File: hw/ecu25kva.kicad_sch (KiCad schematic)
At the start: 0 parts

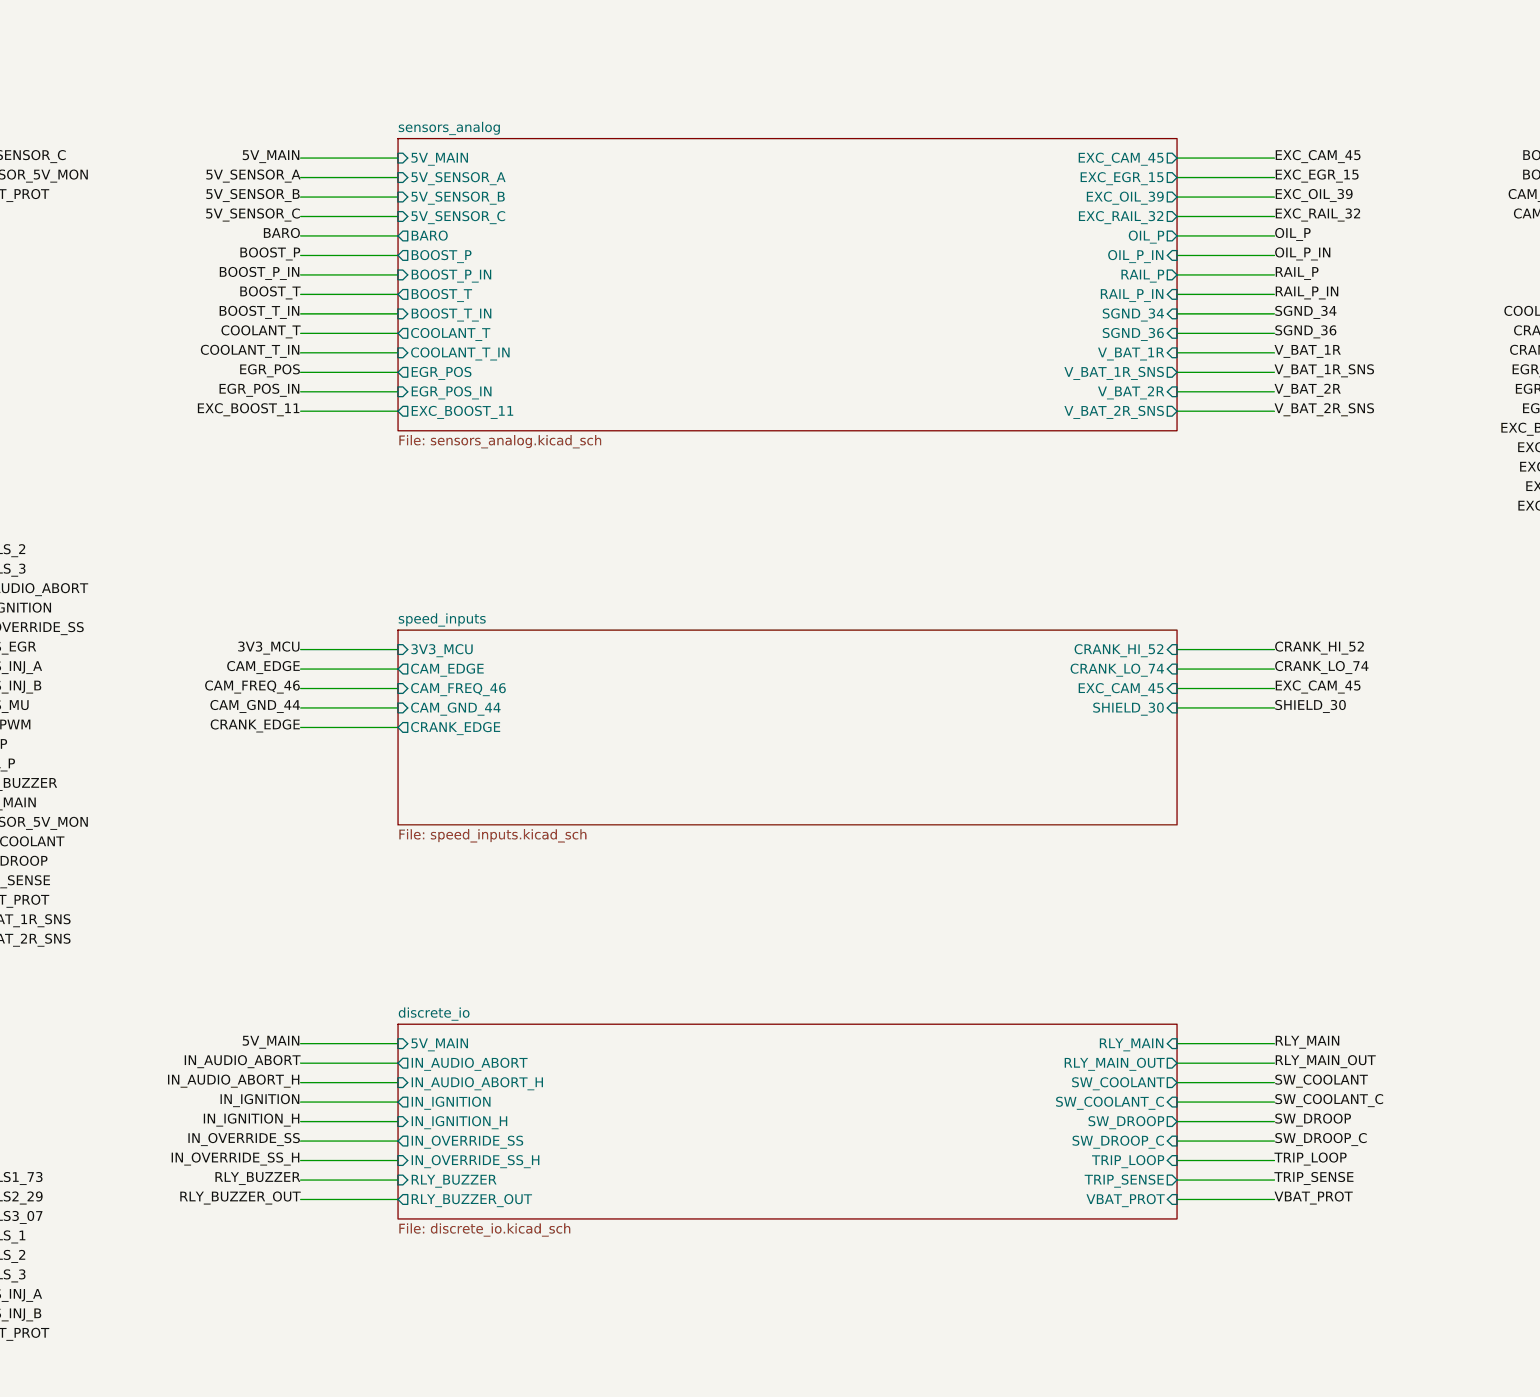
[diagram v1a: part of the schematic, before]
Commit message: Replace the analog-input zeners with BAV199-Q rail clamps
LOWV-CLAMP, analog half. The ten 3.3 V zeners on the sensor and cam
inputs leaked at signal level (the datasheet allows 5 uA at 1 V); they
are now BAV199-Q (80 nA max at 150 C, AEC-Q101) to 3V3_MCU and ground,
drawn as one 3-pin part so each pair is one package. The speed input's
split BAV199 halves and the power-input sense clamp use the same part.

A rail clamp needs something the zener did not: the BAV199's upper
diode is high-Vf, so on a 40 V harness short the MCU pad's ESD diode
would take most of the fault current, over the +/-3 mA injection
limit. Each clamped channel now has 1k between clamp and pad: 0.40 mA
injected. sensor_ratiometric and cam_frontend model the pair, the 1k
and the pad diode, and check the injection current.

The new models also showed the old zener loading the cam signal by
84 mV at a 5.25 V rail -- pinned by the old check as the expected
value. Re-pinned to the divider's own 3.231 V.

The discrete inputs stay open: they clamp continuously, which neither
a rail clamp nor an LM4040-class reference (35 uA bias below
breakdown) can do within the pin's ratings.

24/24 sim blocks, netlist gate passing, 197 R/C packaged.
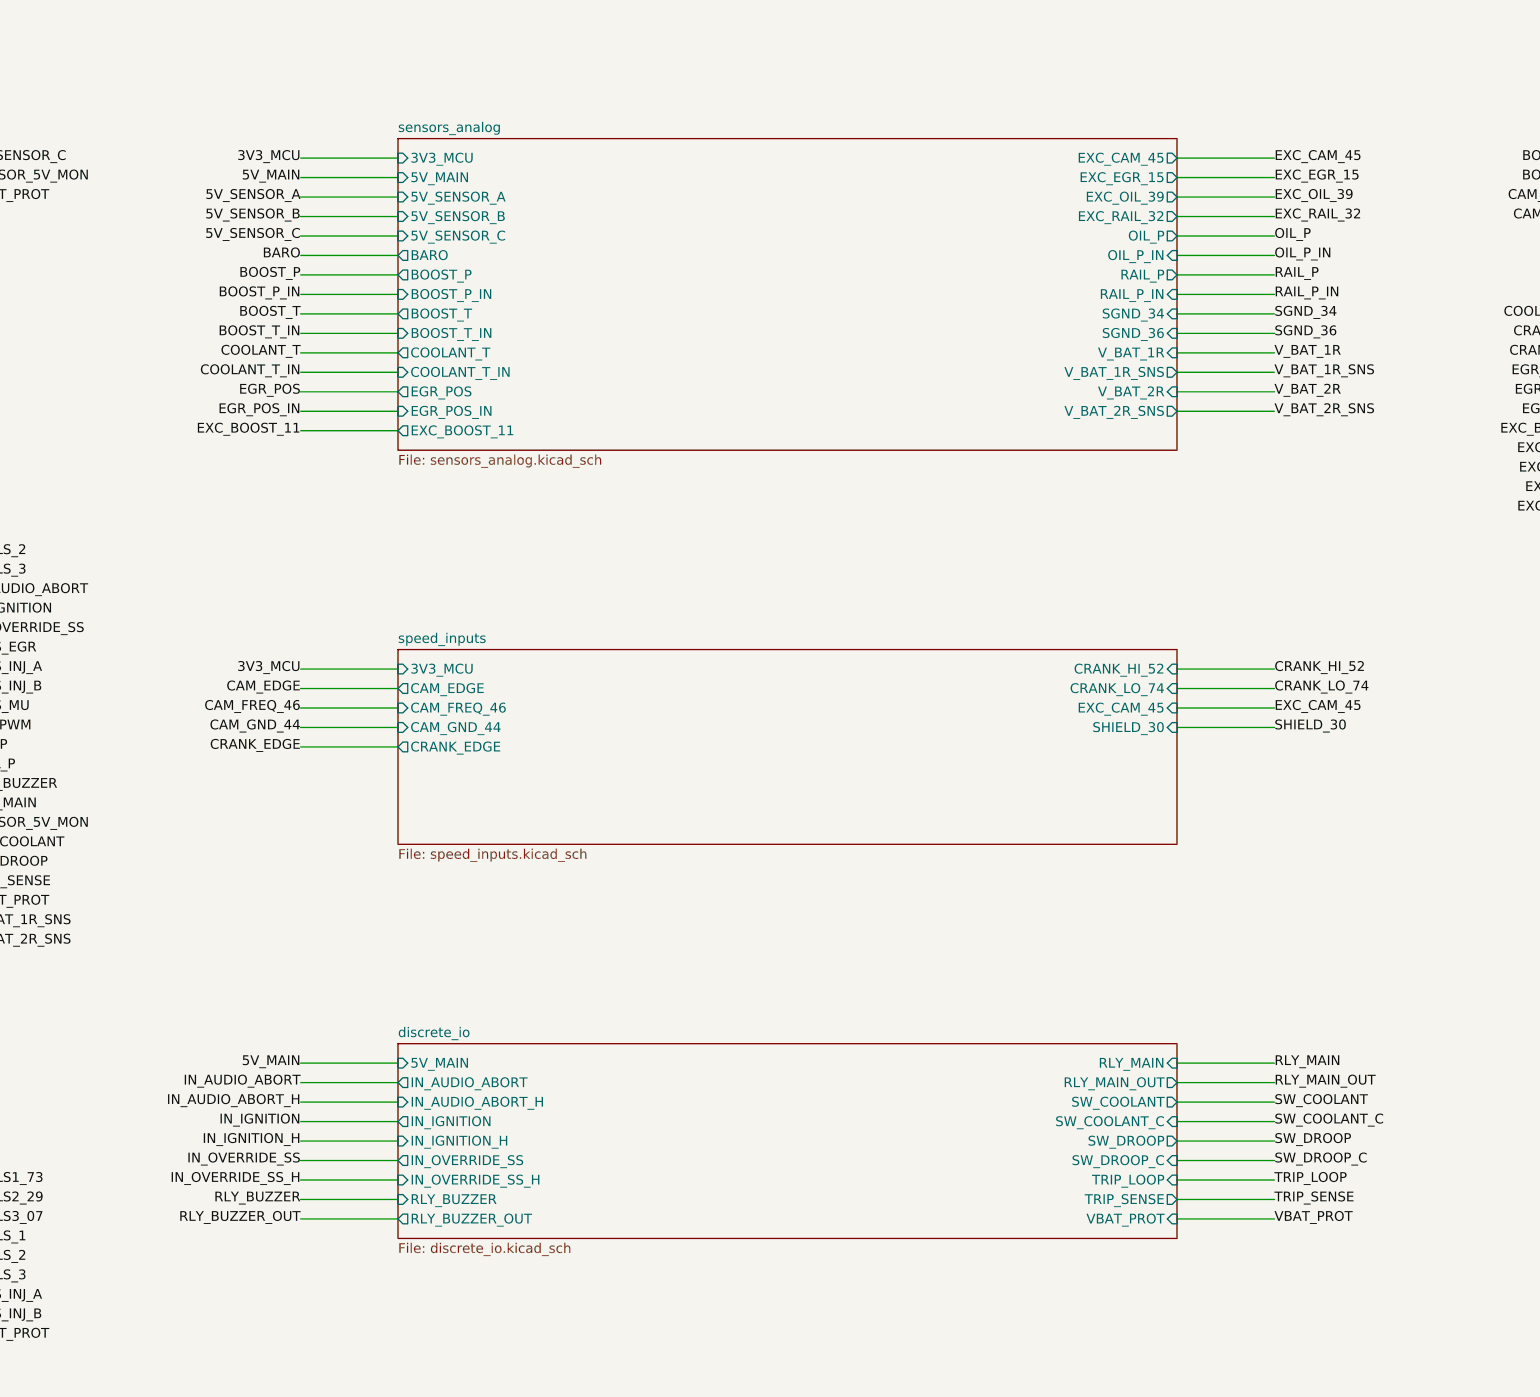
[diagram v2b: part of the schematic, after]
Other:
- sheet sensors_analog ports: added 3V3_MCU; removed none

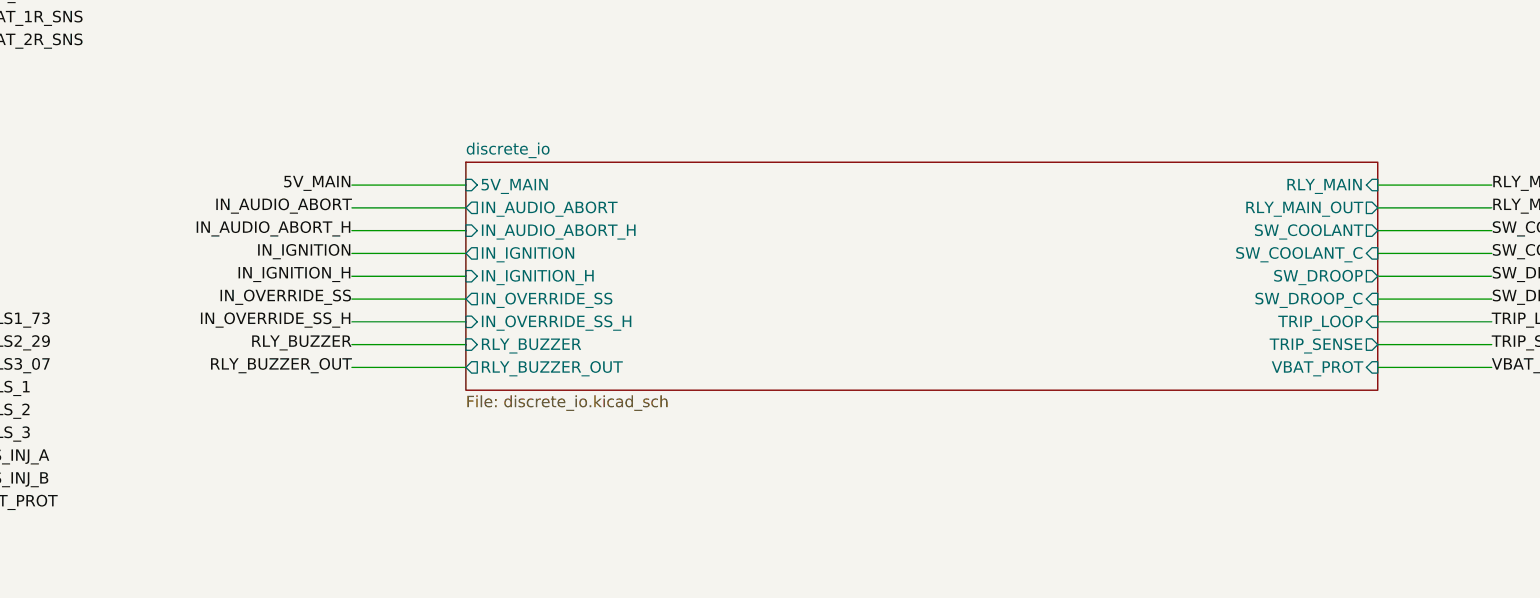
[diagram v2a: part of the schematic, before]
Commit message: Replace the discrete-input clamps with NPN buffers
LOWV-CLAMP, discrete half. The five switch inputs (pins 20/24/71 and
the contact-to-ground 43/23) clamped a 6-40 V input to ~3.0 V
continuously, which no clamp does inside the pad's ratings: a 3.0 V
zener has a soft knee at uA, a BAV199 rail clamp parks the pad at
3.9 V, and an LM4040-class reference draws ~35 uA of bias below
breakdown (TI SNOS633N Fig. 5-4) -- more than the cranking-dip input
could supply.

Each input is now 10k into an NPN base (4.7k + 4.7 uF to ground,
BAV199-Q lower diode against reverse battery), PMBT3904-Q collector to
the pad with 10k to 3V3_MCU. The pad only ever sees 0..3.3 V. Logic is
inverted; pinmap.md records it.

discrete_input.cir is rewritten and checked at the worst corners, not
typical: hFE 30 (datasheet min 60, halved for -40 C) still pulls the
pad to 0.03 V from a 6 V input; a typical part at 125 C stays off below
1.3 V; the base holds -1.05 V on -24 V reverse battery against a 6 V
VEBO; one edge through a 5-chatter bounce. The input resistor is 10k,
not 100k, for 1.1 mA of contact wetting current at 12 V -- 0.11 mA lets
non-gold contacts oxidise open in the field.

Failure modes (transistor open -> stuck inactive, C-E short -> stuck
active) are recorded on the sheet for the firmware plausibility spec.
The trip loop keeps its analog clamp: its healthy band is the clamp
level.

24/24 sim blocks, netlist gate passing, 202 R/C packaged.
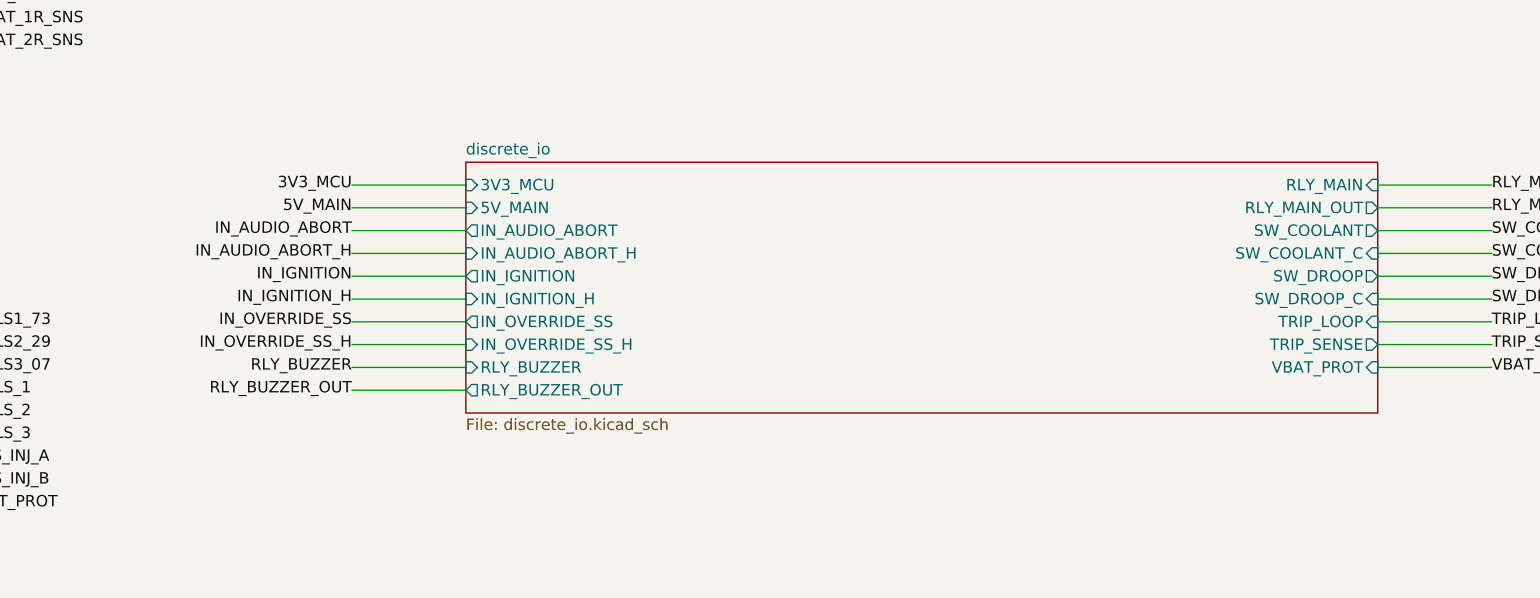
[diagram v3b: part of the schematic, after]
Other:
- sheet discrete_io ports: added 3V3_MCU; removed none
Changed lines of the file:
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@@
     )
   )
-  (sheet (at 215.0 197.44000000000003) (size 101.6 25.40) (fields_autoplaced)
+  (sheet (at 215.0 197.44000000000003) (size 101.6 27.94) (fields_autoplaced)
     (stroke (width 0.1524) (type solid))
     (fill (color 0 0 0 0.0000))
@@
       (effects (font (size 1.27 1.27)) (justify left bottom))
     )
-    (property "Sheetfile" "discrete_io.kicad_sch" (id 1) (at 215.0 223.40 0)
+    (property "Sheetfile" "discrete_io.kicad_sch" (id 1) (at 215.0 225.94 0)
       (effects (font (size 1.27 1.27)) (justify left top))
     )
@@
       (effects (font (size 1.27 1.27)) (justify left) hide)
     )
-    (pin "5V_MAIN" input (at 215.00 199.98 180)
-      (effects (font (size 1.27 1.27)) (justify left))
-    )
-    (pin "IN_AUDIO_ABORT" output (at 215.00 202.52 180)
-      (effects (font (size 1.27 1.27)) (justify left))
-    )
-    (pin "IN_AUDIO_ABORT_H" input (at 215.00 205.06 180)
-      (effects (font (size 1.27 1.27)) (justify left))
-    )
-    (pin "IN_IGNITION" output (at 215.00 207.60 180)
-      (effects (font (size 1.27 1.27)) (justify left))
-    )
-    (pin "IN_IGNITION_H" input (at 215.00 210.14 180)
-      (effects (font (size 1.27 1.27)) (justify left))
-    )
-    (pin "IN_OVERRIDE_SS" output (at 215.00 212.68 180)
-      (effects (font (size 1.27 1.27)) (justify left))
-    )
-    (pin "IN_OVERRIDE_SS_H" input (at 215.00 215.22 180)
-      (effects (font (size 1.27 1.27)) (justify left))
-    )
-    (pin "RLY_BUZZER" input (at 215.00 217.76 180)
-      (effects (font (size 1.27 1.27)) (justify left))
-    )
-    (pin "RLY_BUZZER_OUT" output (at 215.00 220.30 180)
+    (pin "3V3_MCU" input (at 215.00 199.98 180)
+      (effects (font (size 1.27 1.27)) (justify left))
+    )
+    (pin "5V_MAIN" input (at 215.00 202.52 180)
+      (effects (font (size 1.27 1.27)) (justify left))
+    )
+    (pin "IN_AUDIO_ABORT" output (at 215.00 205.06 180)
+      (effects (font (size 1.27 1.27)) (justify left))
+    )
+    (pin "IN_AUDIO_ABORT_H" input (at 215.00 207.60 180)
+      (effects (font (size 1.27 1.27)) (justify left))
+    )
+    (pin "IN_IGNITION" output (at 215.00 210.14 180)
+      (effects (font (size 1.27 1.27)) (justify left))
+    )
+    (pin "IN_IGNITION_H" input (at 215.00 212.68 180)
+      (effects (font (size 1.27 1.27)) (justify left))
+    )
+    (pin "IN_OVERRIDE_SS" output (at 215.00 215.22 180)
+      (effects (font (size 1.27 1.27)) (justify left))
+    )
+    (pin "IN_OVERRIDE_SS_H" input (at 215.00 217.76 180)
+      (effects (font (size 1.27 1.27)) (justify left))
+    )
+    (pin "RLY_BUZZER" input (at 215.00 220.30 180)
+      (effects (font (size 1.27 1.27)) (justify left))
+    )
+    (pin "RLY_BUZZER_OUT" output (at 215.00 222.84 180)
       (effects (font (size 1.27 1.27)) (justify left))
     )
@@
     (stroke (width 0) (type default))
   )
-  (label "5V_MAIN" (at 202.30 199.98 180)
+  (label "3V3_MCU" (at 202.30 199.98 180)
     (effects (font (size 1.27 1.27)) (justify right))
   )
@@
     (stroke (width 0) (type default))
   )
-  (label "IN_AUDIO_ABORT" (at 202.30 202.52 180)
+  (label "5V_MAIN" (at 202.30 202.52 180)
     (effects (font (size 1.27 1.27)) (justify right))
   )
@@
     (stroke (width 0) (type default))
   )
-  (label "IN_AUDIO_ABORT_H" (at 202.30 205.06 180)
+  (label "IN_AUDIO_ABORT" (at 202.30 205.06 180)
     (effects (font (size 1.27 1.27)) (justify right))
   )
@@
     (stroke (width 0) (type default))
   )
-  (label "IN_IGNITION" (at 202.30 207.60 180)
+  (label "IN_AUDIO_ABORT_H" (at 202.30 207.60 180)
     (effects (font (size 1.27 1.27)) (justify right))
   )
@@
     (stroke (width 0) (type default))
   )
-  (label "IN_IGNITION_H" (at 202.30 210.14 180)
+  (label "IN_IGNITION" (at 202.30 210.14 180)
     (effects (font (size 1.27 1.27)) (justify right))
   )
@@
     (stroke (width 0) (type default))
   )
-  (label "IN_OVERRIDE_SS" (at 202.30 212.68 180)
+  (label "IN_IGNITION_H" (at 202.30 212.68 180)
     (effects (font (size 1.27 1.27)) (justify right))
   )
@@
     (stroke (width 0) (type default))
   )
-  (label "IN_OVERRIDE_SS_H" (at 202.30 215.22 180)
+  (label "IN_OVERRIDE_SS" (at 202.30 215.22 180)
     (effects (font (size 1.27 1.27)) (justify right))
   )
@@
     (stroke (width 0) (type default))
   )
-  (label "RLY_BUZZER" (at 202.30 217.76 180)
+  (label "IN_OVERRIDE_SS_H" (at 202.30 217.76 180)
     (effects (font (size 1.27 1.27)) (justify right))
   )
@@
     (stroke (width 0) (type default))
   )
-  (label "RLY_BUZZER_OUT" (at 202.30 220.30 180)
-    (effects (font (size 1.27 1.27)) (justify right))
-  )
+  (label "RLY_BUZZER" (at 202.30 220.30 180)
+    (effects (font (size 1.27 1.27)) (justify right))
+  )
+  (wire (pts (xy 215.00 222.84) (xy 202.30 222.84))
+    (stroke (width 0) (type default))
+  )
+  (label "RLY_BUZZER_OUT" (at 202.30 222.84 180)
+    (effects (font (size 1.27 1.27)) (justify right))
+  )
